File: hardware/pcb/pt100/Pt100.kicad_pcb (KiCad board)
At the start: 2 copper layers, 44 x 29 mm, 21 parts, among them J1 AudioJack3, U1 OPA2340, U2 OPA2340

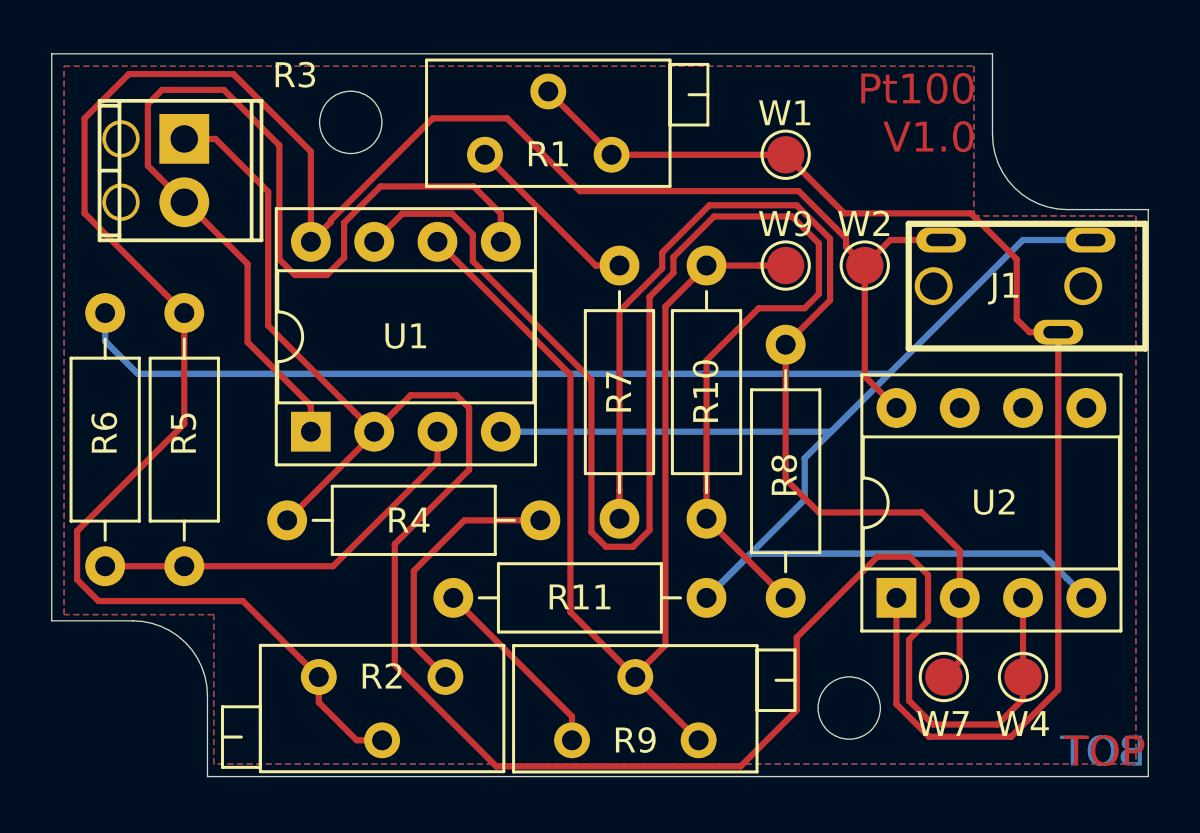
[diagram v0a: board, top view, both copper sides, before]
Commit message: feat: General PCB improvements
use old stuff

Issue #14
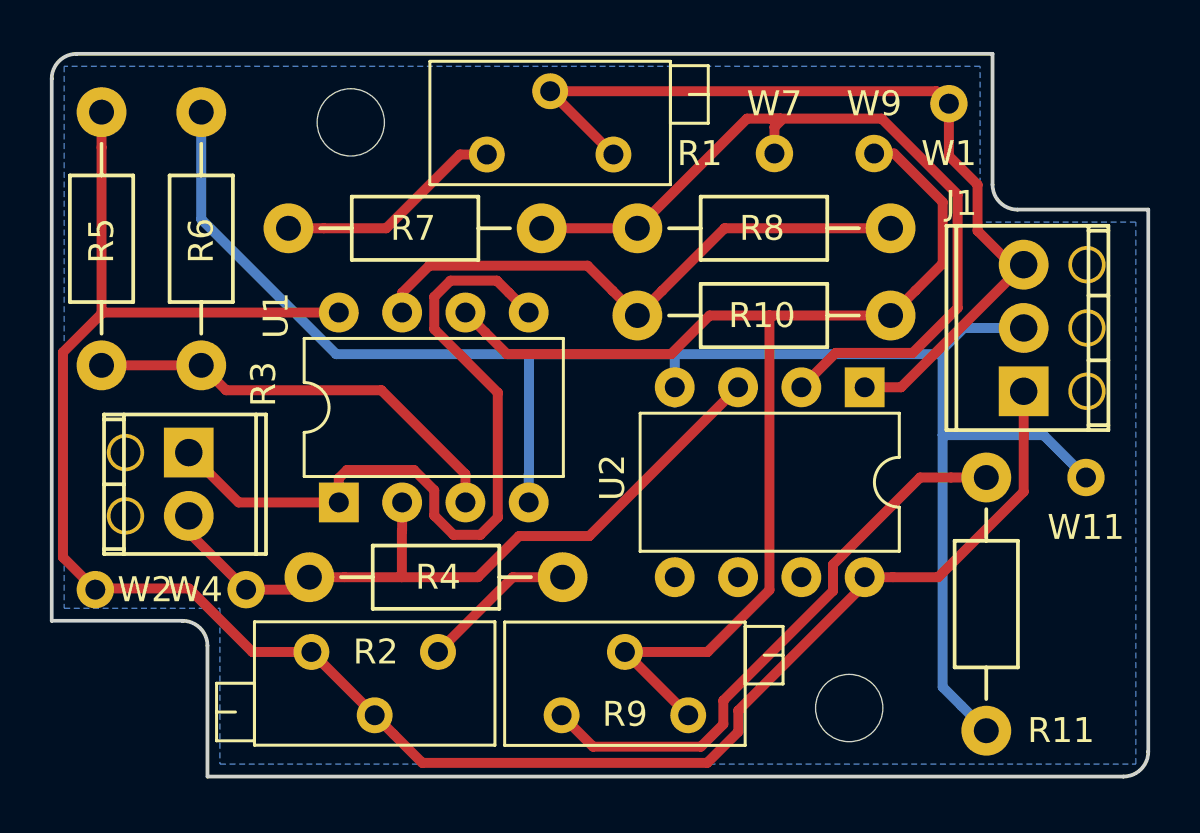
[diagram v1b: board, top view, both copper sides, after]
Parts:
- removed the ~ at (27.0, 17.8)
- removed the ~ at (47.0, 41.2)
- added W11: TEST_11P, Measurement_Points:Measurement_Point_Round-TH_Small, F.Cu at (56.5, 32.0)
- added ~: MountingHole_2.7mm_M2.5, Mounting_Holes:MountingHole_2.7mm_M2.5, F.Cu at (47.0, 41.2)
- added ~: MountingHole_2.7mm_M2.5, Mounting_Holes:MountingHole_2.7mm_M2.5, F.Cu at (27.0, 17.8)
- J1: value AudioJack3 -> JACK_TRS_3PINS; footprint Lumberg:LUMBERG_1501_03 -> Pheonix:TerminalBlock_Pheonix_MPT-2.54mm_3pol
- R1, R2, R9: footprint Potentiometer_THT:Potentiometer_Bourns_3296Z_Horizontal -> Potentiometers:Potentiometer_Trimmer_Bourns_3296Z
- R10, R11, R4, R5, R6, R7, R8: footprint Resistor_THT:R_Axial_DIN0207_L6.3mm_D2.5mm_P10.16mm_Horizontal -> ThroughHole:Resistor_Horizontal_RM10mm
- R3: value PT100 -> THERMISTOR
- U1, U2: footprint Package_DIP:DIP-8_W7.62mm_Socket -> Housings_DIP:DIP-8_W7.62mm
- W1: value ~ -> TEST_1P; footprint TestPoint:TestPoint_Pad_D1.5mm -> Measurement_Points:Measurement_Point_Round-TH_Small
- W2: value ~ -> TEST_2P; footprint TestPoint:TestPoint_Pad_D1.5mm -> Measurement_Points:Measurement_Point_Round-TH_Small
- W4: value ~ -> TEST_4P; footprint TestPoint:TestPoint_Pad_D1.5mm -> Measurement_Points:Measurement_Point_Round-TH_Small
- W7: value ~ -> TEST_7P; footprint TestPoint:TestPoint_Pad_D1.5mm -> Measurement_Points:Measurement_Point_Round-TH_Small
- W9: value ~ -> TEST_9P; footprint TestPoint:TestPoint_Pad_D1.5mm -> Measurement_Points:Measurement_Point_Round-TH_Small
- moved W2 33.5 mm to (16.8, 36.5)
- moved W4 31.4 mm to (22.8, 36.5)
- moved W7 22.1 mm to (44.0, 19.0)
- moved R11 22.0 mm to (52.5, 42.2), turned to 90 degrees
- moved R3 12.6 mm to (20.5, 31.0)
- moved R10 11.0 mm to (48.7, 25.5), turned to 180 degrees
- moved R4 9.54 mm to (25.3, 36.0), turned to 0 degrees
- moved R6 8.93 mm to (21.0, 17.3)
- moved U2 8.55 mm to (47.6, 28.4), turned to 270 degrees
- moved W1 6.86 mm to (51.0, 17.0)
- moved R8 6.29 mm to (48.7, 22.0), turned to 180 degrees
- moved W9 5.73 mm to (48.0, 19.0)
- moved J1 4.85 mm to (54.0, 28.5), turned to 90 degrees
- moved R5 3.93 mm to (17.0, 27.5), turned to 90 degrees
- moved R7 3.46 mm to (34.7, 22.0), turned to 180 degrees
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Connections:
- R1 pad 2: /SIGNAL -> /SIGNAL_T1
- R1 pad 3: /SIGNAL -> /SIGNAL_T1
- R11 pad 1: Net-(R11-Pad1) -> AGND
- R11 pad 2: GND -> Net-(R11-Pad2)
- R4 pad 1: Net-(R2-Pad1) -> Net-(R3-Pad2)
- R4 pad 2: Net-(R3-Pad1) -> Net-(R2-Pad1)
- R5 pad 1: +5V -> Net-(R5-Pad1)
- R5 pad 2: Net-(R5-Pad2) -> +5V
- R6 pad 1: GND -> AGND
- R6 pad 2: Net-(R5-Pad2) -> Net-(R5-Pad1)
- R7 pad 1: Net-(R1-Pad1) -> Net-(R7-Pad1)
- R7 pad 2: Net-(R7-Pad2) -> Net-(R1-Pad1)
- R8 pad 1: Net-(R7-Pad2) -> Net-(R10-Pad2)
- R8 pad 2: Net-(R10-Pad1) -> Net-(R7-Pad1)
- R9 pad 1: Net-(R11-Pad1) -> Net-(R11-Pad2)
- R9 pad 2: Net-(R10-Pad2) -> Net-(R10-Pad1)
- R9 pad 3: Net-(R10-Pad2) -> Net-(R10-Pad1)
- U1 pad 1: Net-(R3-Pad2) -> Net-(R3-Pad1)
- U1 pad 2: Net-(R3-Pad1) -> Net-(R3-Pad2)
- U1 pad 3: Net-(R5-Pad2) -> Net-(R5-Pad1)
- U1 pad 4: GND -> AGND
- U1 pad 5: Net-(R3-Pad2) -> Net-(R3-Pad1)
- U1 pad 6: Net-(R10-Pad2) -> Net-(R10-Pad1)
- U1 pad 7: Net-(R10-Pad1) -> Net-(R10-Pad2)
- U2 pad 1: /SIGNAL -> /SIGNAL_T1
- U2 pad 2: Net-(R7-Pad2) -> Net-(R7-Pad1)
- U2 pad 3: Net-(R3-Pad1) -> Net-(R3-Pad2)
- U2 pad 4: GND -> AGND
- U2 pad 5: Net-(U2-Pad5) -> (no net)
- U2 pad 6: Net-(U2-Pad6) -> (no net)
- U2 pad 7: Net-(U2-Pad7) -> (no net)
- W1 pad 1: /SIGNAL -> /SIGNAL_T1
- W4 pad 1: Net-(R3-Pad1) -> Net-(R3-Pad2)
- W7 pad 1: Net-(R7-Pad2) -> Net-(R7-Pad1)
- W9 pad 1: Net-(R10-Pad2) -> Net-(R10-Pad1)
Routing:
- net GND: track 87.6 -> 0.00 mm
- net AGND: track 0.00 -> 71.5 mm, vias 0 -> 1
- net /SIGNAL: track 52.3 -> 0.00 mm
- net Net-(R3-Pad1): track 80.2 -> 30.8 mm
- net Net-(R7-Pad2): track 43.4 -> 0.00 mm
- net /SIGNAL_T1: track 0.00 -> 37.0 mm
- net Net-(R7-Pad1): track 0.00 -> 33.8 mm
- net Net-(R11-Pad2): track 0.00 -> 23.2 mm
- net Net-(R10-Pad2): track 45.2 -> 23.1 mm
- net Net-(R5-Pad1): track 0.00 -> 17.5 mm
- net Net-(R5-Pad2): track 16.3 -> 0.00 mm
- net +5V: track 88.9 -> 79.3 mm
- net Net-(R10-Pad1): track 58.3 -> 49.1 mm
- net Net-(R3-Pad2): track 39.9 -> 30.7 mm
- net Net-(R11-Pad1): track 7.69 -> 0.00 mm
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- added copper zone on B.Cu, net AGND
- removed copper zone on F.Cu, net +5V
- removed copper zone on B.Cu, net GND
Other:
- outline, holes or cut-outs redrawn
- net class Default: trace_width 0.25 -> 0.4; via_dia 0.8 -> 0.6
- rule pad_to_mask_clearance: 0.051 -> 0.2
- board text removed: "BOT"
- board text removed: "Pt100 V1.0"
- board text removed: "TOP"
